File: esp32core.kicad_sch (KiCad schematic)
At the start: 1 part

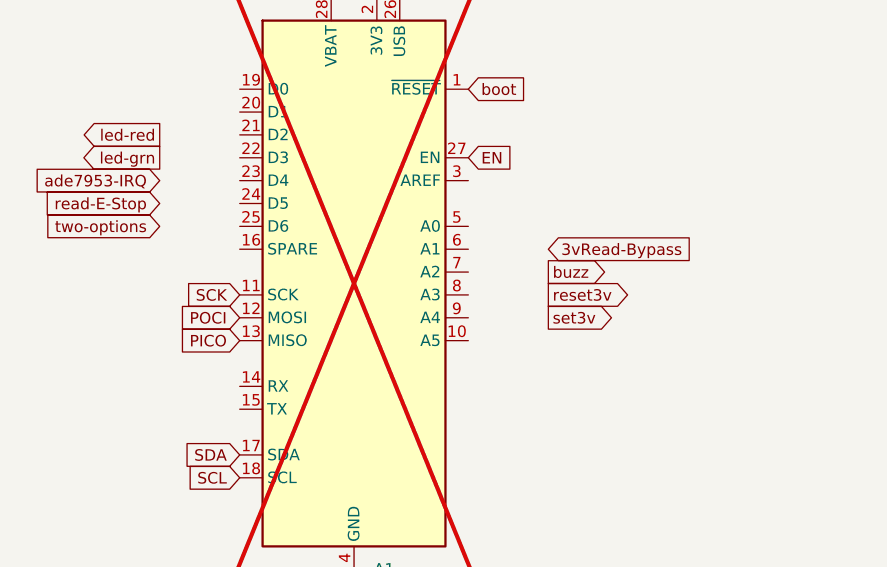
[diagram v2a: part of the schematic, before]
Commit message: [fix] PICO/POCI flipped on Feather Boards
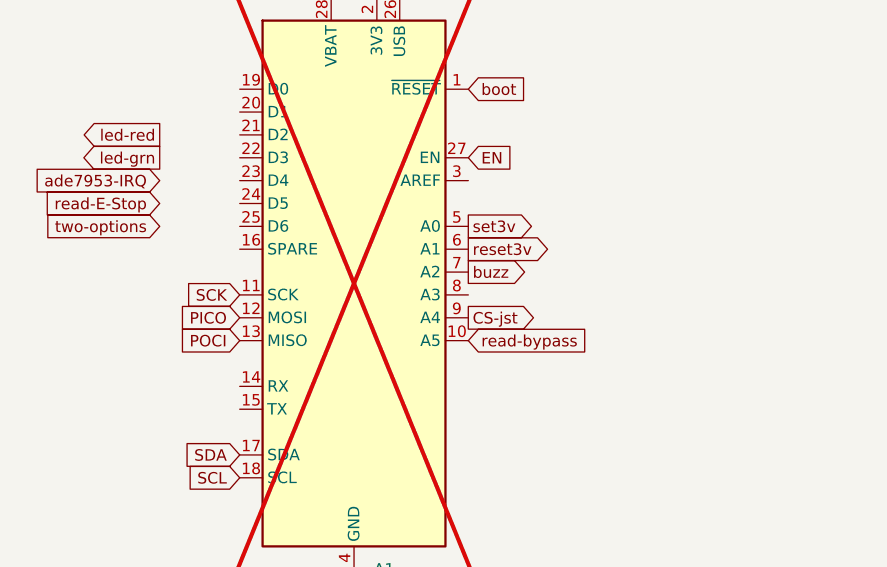
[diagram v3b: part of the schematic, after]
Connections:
- net PICO: now also A1.12 (MOSI); no longer A1.13 (MISO)
- net POCI: now also A1.13 (MISO); no longer A1.12 (MOSI)
- net buzz: now also A1.7 (A2)
- net reset3v: now also A1.6 (A1)
- net set3v: now also A1.5 (A0)
- net read-bypass: now reaches A1.10 (A5)
- net CS-jst: now reaches A1.9 (A4)
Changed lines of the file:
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@@
 	(global_label "POCI"
 		(shape input)
+		(at 175.26 114.3 180)
+		(fields_autoplaced yes)
+		(effects
+			(font
+				(size 1.27 1.27)
+			)
+			(justify right)
+		)
+		(property "Intersheetrefs" "${INTERSHEET_REFS}"
+			(at 167.7995 114.3 0)
+			(effects
+				(font
+					(size 1.27 1.27)
+				)
+				(justify right)
+				(hide yes)
+			)
+		)
+	)
+	(global_label "CS-jst"
+		(shape output)
+		(at 200.66 111.76 0)
+		(fields_autoplaced yes)
+		(effects
+			(font
+				(size 1.27 1.27)
+			)
+			(justify left)
+		)
+		(property "Intersheetrefs" "${INTERSHEET_REFS}"
+			(at 210.0557 111.76 0)
+			(effects
+				(font
+					(size 1.27 1.27)
+				)
+				(justify left)
+				(hide yes)
+			)
+		)
+	)
+	(global_label "SDA"
+		(shape input)
+		(at 175.26 127 180)
+		(fields_autoplaced yes)
+		(effects
+			(font
+				(size 1.27 1.27)
+			)
+			(justify right)
+		)
+		(property "Intersheetrefs" "${INTERSHEET_REFS}"
+			(at 168.7067 127 0)
+			(effects
+				(font
+					(size 1.27 1.27)
+				)
+				(justify right)
+				(hide yes)
+			)
+		)
+	)
+	(global_label "EN"
+		(shape input)
+		(at 200.66 93.98 0)
+		(fields_autoplaced yes)
+		(effects
+			(font
+				(size 1.27 1.27)
+			)
+			(justify left)
+		)
+		(property "Intersheetrefs" "${INTERSHEET_REFS}"
+			(at 206.1247 93.98 0)
+			(effects
+				(font
+					(size 1.27 1.27)
+				)
+				(justify left)
+				(hide yes)
+			)
+		)
+	)
+	(global_label "led-red"
+		(shape output)
+		(at 166.37 91.44 180)
+		(fields_autoplaced yes)
+		(effects
+			(font
+				(size 1.27 1.27)
+			)
+			(justify right)
+		)
+		(property "Intersheetrefs" "${INTERSHEET_REFS}"
+			(at 156.4579 91.3606 0)
+			(effects
+				(font
+					(size 1.27 1.27)
+				)
+				(justify right)
+				(hide yes)
+			)
+		)
+	)
+	(global_label "SCK"
+		(shape input)
+		(at 175.26 109.22 180)
+		(fields_autoplaced yes)
+		(effects
+			(font
+				(size 1.27 1.27)
+			)
+			(justify right)
+		)
+		(property "Intersheetrefs" "${INTERSHEET_REFS}"
+			(at 168.5253 109.22 0)
+			(effects
+				(font
+					(size 1.27 1.27)
+				)
+				(justify right)
+				(hide yes)
+			)
+		)
+	)
+	(global_label "two-options"
+		(shape input)
+		(at 166.37 101.6 180)
+		(fields_autoplaced yes)
+		(effects
+			(font
+				(size 1.27 1.27)
+			)
+			(justify right)
+		)
+		(property "Intersheetrefs" "${INTERSHEET_REFS}"
+			(at 152.2245 101.5206 0)
+			(effects
+				(font
+					(size 1.27 1.27)
+				)
+				(justify right)
+				(hide yes)
+			)
+		)
+	)
+	(global_label "PICO"
+		(shape input)
 		(at 175.26 111.76 180)
 		(fields_autoplaced yes)
@@
 		)
 	)
-	(global_label "SDA"
-		(shape input)
-		(at 175.26 127 180)
-		(fields_autoplaced yes)
-		(effects
-			(font
-				(size 1.27 1.27)
-			)
-			(justify right)
-		)
-		(property "Intersheetrefs" "${INTERSHEET_REFS}"
-			(at 168.7067 127 0)
-			(effects
-				(font
-					(size 1.27 1.27)
-				)
-				(justify right)
-				(hide yes)
-			)
-		)
-	)
-	(global_label "EN"
-		(shape input)
-		(at 200.66 93.98 0)
-		(fields_autoplaced yes)
-		(effects
-			(font
-				(size 1.27 1.27)
-			)
-			(justify left)
-		)
-		(property "Intersheetrefs" "${INTERSHEET_REFS}"
-			(at 206.1247 93.98 0)
-			(effects
-				(font
-					(size 1.27 1.27)
-				)
-				(justify left)
-				(hide yes)
-			)
-		)
-	)
-	(global_label "led-red"
-		(shape output)
-		(at 166.37 91.44 180)
-		(fields_autoplaced yes)
-		(effects
-			(font
-				(size 1.27 1.27)
-			)
-			(justify right)
-		)
-		(property "Intersheetrefs" "${INTERSHEET_REFS}"
-			(at 156.4579 91.3606 0)
-			(effects
-				(font
-					(size 1.27 1.27)
-				)
-				(justify right)
-				(hide yes)
-			)
-		)
-	)
-	(global_label "SCK"
-		(shape input)
-		(at 175.26 109.22 180)
-		(fields_autoplaced yes)
-		(effects
-			(font
-				(size 1.27 1.27)
-			)
-			(justify right)
-		)
-		(property "Intersheetrefs" "${INTERSHEET_REFS}"
-			(at 168.5253 109.22 0)
-			(effects
-				(font
-					(size 1.27 1.27)
-				)
-				(justify right)
-				(hide yes)
-			)
-		)
-	)
-	(global_label "two-options"
-		(shape input)
-		(at 166.37 101.6 180)
-		(fields_autoplaced yes)
-		(effects
-			(font
-				(size 1.27 1.27)
-			)
-			(justify right)
-		)
-		(property "Intersheetrefs" "${INTERSHEET_REFS}"
-			(at 152.2245 101.5206 0)
-			(effects
-				(font
-					(size 1.27 1.27)
-				)
-				(justify right)
-				(hide yes)
-			)
-		)
-	)
-	(global_label "PICO"
-		(shape input)
-		(at 175.26 114.3 180)
-		(fields_autoplaced yes)
-		(effects
-			(font
-				(size 1.27 1.27)
-			)
-			(justify right)
-		)
-		(property "Intersheetrefs" "${INTERSHEET_REFS}"
-			(at 167.7995 114.3 0)
-			(effects
-				(font
-					(size 1.27 1.27)
-				)
-				(justify right)
-				(hide yes)
-			)
-		)
-	)
 	(global_label "ade7953-IRQ"
 		(shape input)
@@
 	(global_label "reset3v"
 		(shape output)
-		(at 209.55 109.22 0)
-		(fields_autoplaced yes)
-		(effects
-			(font
-				(size 1.27 1.27)
-			)
-			(justify left)
-		)
-		(property "Intersheetrefs" "${INTERSHEET_REFS}"
-			(at 218.8574 109.2994 0)
+		(at 200.66 104.14 0)
+		(fields_autoplaced yes)
+		(effects
+			(font
+				(size 1.27 1.27)
+			)
+			(justify left)
+		)
+		(property "Intersheetrefs" "${INTERSHEET_REFS}"
+			(at 209.9674 104.2194 0)
+			(effects
+				(font
+					(size 1.27 1.27)
+				)
+				(justify left)
+				(hide yes)
+			)
+		)
+	)
+	(global_label "read-bypass"
+		(shape input)
+		(at 200.66 114.3 0)
+		(fields_autoplaced yes)
+		(effects
+			(font
+				(size 1.27 1.27)
+			)
+			(justify left)
+		)
+		(property "Intersheetrefs" "${INTERSHEET_REFS}"
+			(at 215.8612 114.3 0)
 			(effects
 				(font
@@
 	(global_label "buzz"
 		(shape output)
-		(at 209.55 106.68 0)
-		(fields_autoplaced yes)
-		(effects
-			(font
-				(size 1.27 1.27)
-			)
-			(justify left)
-		)
-		(property "Intersheetrefs" "${INTERSHEET_REFS}"
-			(at 216.3174 106.6006 0)
+		(at 200.66 106.68 0)
+		(fields_autoplaced yes)
+		(effects
+			(font
+				(size 1.27 1.27)
+			)
+			(justify left)
+		)
+		(property "Intersheetrefs" "${INTERSHEET_REFS}"
+			(at 207.4274 106.6006 0)
 			(effects
 				(font
@@
 	(global_label "set3v"
 		(shape output)
-		(at 209.55 111.76 0)
-		(fields_autoplaced yes)
-		(effects
-			(font
-				(size 1.27 1.27)
-			)
-			(justify left)
-		)
-		(property "Intersheetrefs" "${INTERSHEET_REFS}"
-			(at 216.9826 111.6806 0)
-			(effects
-				(font
-					(size 1.27 1.27)
-				)
-				(justify left)
-				(hide yes)
-			)
-		)
-	)
-	(global_label "3vRead-Bypass"
-		(shape input)
-		(at 209.55 104.14 0)
-		(fields_autoplaced yes)
-		(effects
-			(font
-				(size 1.27 1.27)
-			)
-			(justify left)
-		)
-		(property "Intersheetrefs" "${INTERSHEET_REFS}"
-			(at 227.5331 104.14 0)
-			(effects
-				(font
+		(at 200.66 101.6 0)
+		(fields_autoplaced yes)
+		(effects
+			(font
+				(size 1.27 1.27)
+			)
+			(justify left)
+		)
+		(property "Intersheetrefs" "${INTERSHEET_REFS}"
+			(at 208.0926 101.5206 0)
+			(effects
+				(font

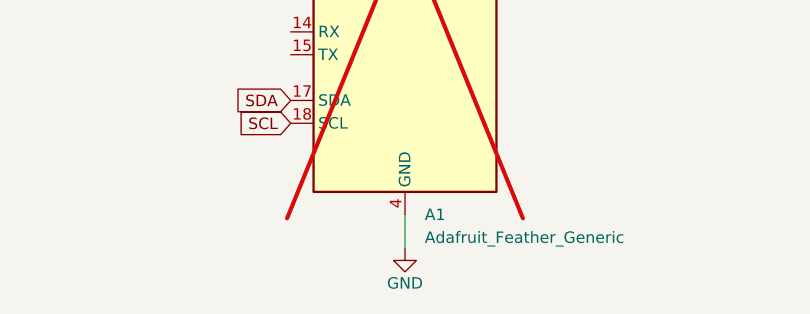
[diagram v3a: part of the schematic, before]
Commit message: added USBC for power. Changed Feather power-supply to be incompliance with Feather's recommendations
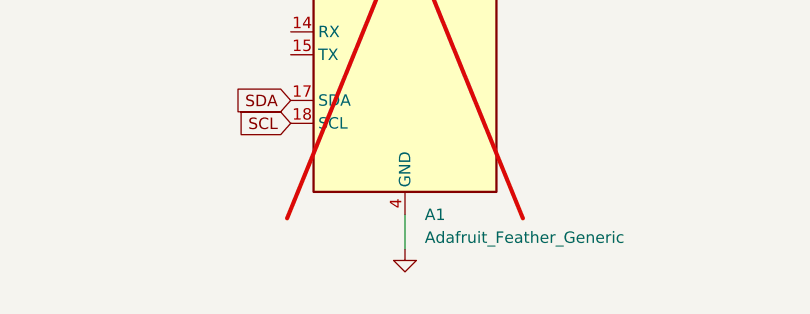
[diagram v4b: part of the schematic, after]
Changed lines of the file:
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@@
 					(size 1.27 1.27)
 				)
+				(hide yes)
 			)
 		)

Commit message: 1.4.1 schematic update
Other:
- note added: "This shows a component to represent the Feather Footprint board, as it will be seated in place. However, the component itself is not included on the circuit board, instead seating into some breakout headers for easy replacement. This page is for reference only, not design. ------------- We love Feather boards because it is a specification, not just a single vendor (but we <3 Adafruit). That way w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"
- note removed: "This shows a component to represent the Feather Footprint board, as it will be seated in place. However, the component itself is not included on the circuit board, instead seating into some breakout headers for easy replacement. This page is for reference only, not design."
- moved on the sheet: A1

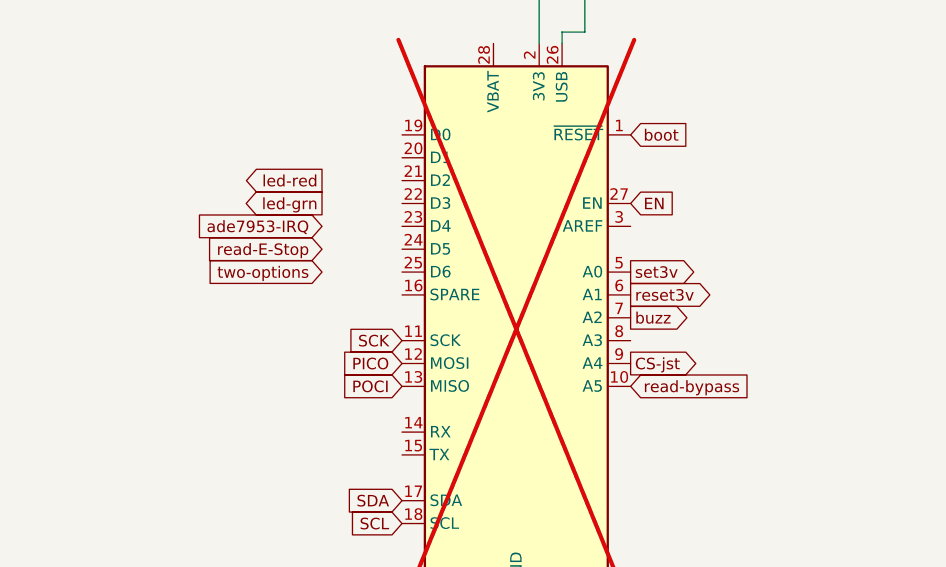
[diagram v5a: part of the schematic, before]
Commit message: 5v binary current and cleanup
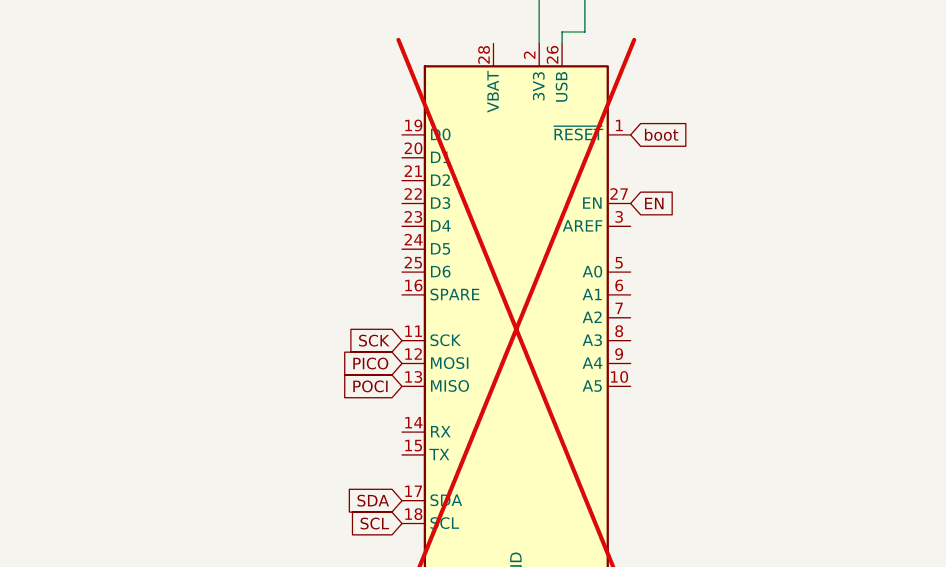
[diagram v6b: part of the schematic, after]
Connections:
- net CS-jst: no longer names the net of A1.9 (A4)
- net buzz: no longer names the net of A1.7 (A2)
- net read-bypass: no longer names the net of A1.10 (A5)
- net reset3v: no longer names the net of A1.6 (A1)
- net set3v: no longer names the net of A1.5 (A0)
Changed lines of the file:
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@@
-		)
-	)
-	(global_label "CS-jst"
-		(shape output)
-		(at 213.36 115.57 0)
-		(fields_autoplaced yes)
-		(effects
-			(font
-				(size 1.27 1.27)
-			)
-			(justify left)
-		)
-		(property "Intersheetrefs" "${INTERSHEET_REFS}"
-			(at 222.7557 115.57 0)
-			(effects
-				(font
-					(size 1.27 1.27)
-				)
-				(justify left)
-				(hide yes)
-			)
 		)
 	)
@@
 		)
 	)
-	(global_label "led-red"
-		(shape output)
-		(at 179.07 95.25 180)
-		(fields_autoplaced yes)
-		(effects
-			(font
-				(size 1.27 1.27)
-			)
-			(justify right)
-		)
-		(property "Intersheetrefs" "${INTERSHEET_REFS}"
-			(at 169.1579 95.1706 0)
-			(effects
-				(font
-					(size 1.27 1.27)
-				)
-				(justify right)
-				(hide yes)
-			)
-		)
-	)
 	(global_label "SCK"
 		(shape input)
@@
 		(property "Intersheetrefs" "${INTERSHEET_REFS}"
 			(at 181.2253 113.03 0)
-			(effects
-				(font
-					(size 1.27 1.27)
-				)
-				(justify right)
-				(hide yes)
-			)
-		)
-	)
-	(global_label "two-options"
-		(shape input)
-		(at 179.07 105.41 180)
-		(fields_autoplaced yes)
-		(effects
-			(font
-				(size 1.27 1.27)
-			)
-			(justify right)
-		)
-		(property "Intersheetrefs" "${INTERSHEET_REFS}"
-			(at 164.9245 105.3306 0)
 			(effects
 				(font
@@
 		)
 	)
-	(global_label "ade7953-IRQ"
-		(shape input)
-		(at 179.07 100.33 180)
-		(fields_autoplaced yes)
-		(effects
-			(font
-				(size 1.27 1.27)
-			)
-			(justify right)
-		)
-		(property "Intersheetrefs" "${INTERSHEET_REFS}"
-			(at 163.6545 100.2506 0)
-			(effects
-				(font
-					(size 1.27 1.27)
-				)
-				(justify right)
-				(hide yes)
-			)
-		)
-	)
-	(global_label "led-grn"
-		(shape output)
-		(at 179.07 97.79 180)
-		(fields_autoplaced yes)
-		(effects
-			(font
-				(size 1.27 1.27)
-			)
-			(justify right)
-		)
-		(property "Intersheetrefs" "${INTERSHEET_REFS}"
-			(at 169.0974 97.7106 0)
-			(effects
-				(font
-					(size 1.27 1.27)
-				)
-				(justify right)
-				(hide yes)
-			)
-		)
-	)
 	(global_label "boot"
 		(shape input)
@@
 			(effects
 				(font
-					(size 1.27 1.27)
-				)
-				(justify left)
-				(hide yes)
-			)
-		)
-	)
-	(global_label "reset3v"
-		(shape output)
-		(at 213.36 107.95 0)
-		(fields_autoplaced yes)
-		(effects
-			(font
-				(size 1.27 1.27)
-			)
-			(justify left)
-		)
-		(property "Intersheetrefs" "${INTERSHEET_REFS}"
-			(at 222.6674 108.0294 0)
-			(effects
-				(font
-					(size 1.27 1.27)
-				)
-				(justify left)
-				(hide yes)
-			)
-		)
-	)
-	(global_label "read-bypass"
-		(shape input)
-		(at 213.36 118.11 0)
-		(fields_autoplaced yes)
-		(effects
-			(font
-				(size 1.27 1.27)
-			)
-			(justify left)
-		)
-		(property "Intersheetrefs" "${INTERSHEET_REFS}"
-			(at 228.5612 118.11 0)
-			(effects
-				(font
-					(size 1.27 1.27)
-				)
-				(justify left)
-				(hide yes)
-			)
-		)
-	)
-	(global_label "read-E-Stop"
-		(shape input)
-		(at 179.07 102.87 180)
-		(fields_autoplaced yes)
-		(effects
-			(font
-				(size 1.27 1.27)
-			)
-			(justify right)
-		)
-		(property "Intersheetrefs" "${INTERSHEET_REFS}"
-			(at 163.9569 102.7906 0)
-			(effects
-				(font
-					(size 1.27 1.27)
-				)
-				(justify right)
-				(hide yes)
-			)
-		)
-	)
-	(global_label "buzz"
-		(shape output)
-		(at 213.36 110.49 0)
-		(fields_autoplaced yes)
-		(effects
-			(font
-				(size 1.27 1.27)
-			)
-			(justify left)
-		)
-		(property "Intersheetrefs" "${INTERSHEET_REFS}"
-			(at 220.1274 110.4106 0)
-			(effects
-				(font
-					(size 1.27 1.27)
-				)
-				(justify left)
-				(hide yes)
-			)
-		)
-	)
-	(global_label "set3v"
-		(shape output)
-		(at 213.36 105.41 0)
-		(fields_autoplaced yes)
-		(effects
-			(font
-				(size 1.27 1.27)
-			)
-			(justify left)
-		)
-		(property "Intersheetrefs" "${INTERSHEET_REFS}"
-			(at 220.7926 105.3306 0)
-			(effects
-				(font

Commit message: close enough for 3D export
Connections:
- net read-bypass: now reaches A1.10 (A5)
- net led-grn: now reaches A1.19 (D6)
- net led-red: now reaches A1.20 (D5)
- net DC-read-stage2: now reaches A1.21 (D9)
- net CS-eth0: now reaches A1.22 (D10)
- net ade7953-IRQ: now reaches A1.23 (D11)
- net two-options: now reaches A1.24 (D12)
- net read-E-Stop: now reaches A1.25 (D13)
- net set3v: now reaches A1.5 (A0)
- net reset3v: now reaches A1.6 (A1)
- net buzz: now reaches A1.7 (A2)
- net binary-current: now reaches A1.8 (A3)
- net CS-jst: now reaches A1.9 (A4)
- net +3V3: no longer names the net of A1.2 (3V3)
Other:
- note added: "**Use input [not input_pullup]"
- note added: "*Use input_pullup* *invert logic*"
- note added: "IRQ (also maybe not needed)----> https://learn.adafruit.com/ adafruit-wiz5500-wiznet- ethernet-featherwing/pinouts"
- note added: "eth-wng-rst **if not using binary current"
- moved on the sheet: A1
